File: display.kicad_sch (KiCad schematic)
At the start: 3 parts, among them J3 AXF5D3012

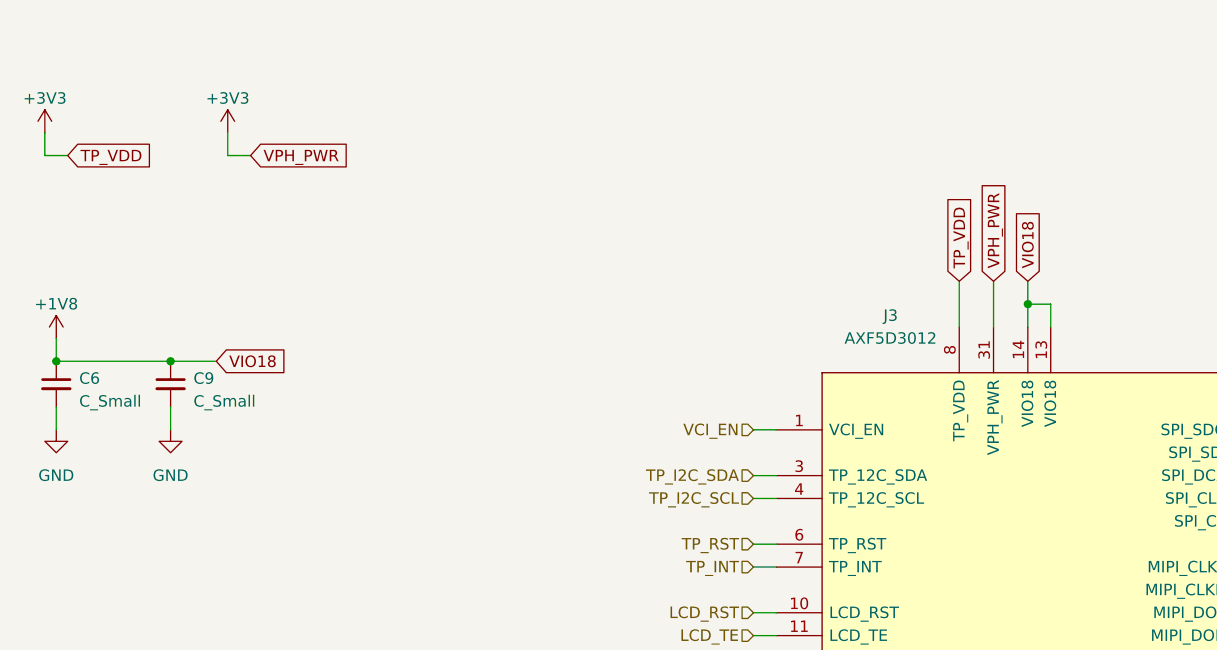
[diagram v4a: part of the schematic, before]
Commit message: cleaned up supply labels
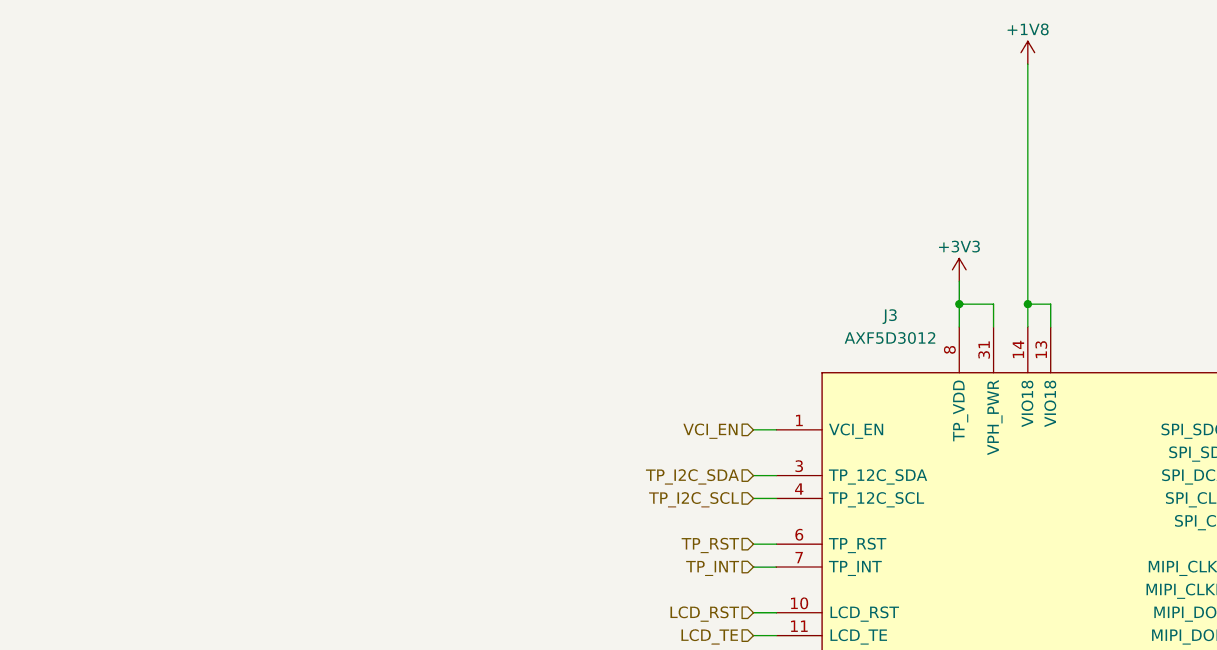
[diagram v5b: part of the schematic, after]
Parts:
- removed C6, C9: C_Small, symbol Device:C_Small

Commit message: cleaned up symbol fields table and removed unused or duplicate fields.
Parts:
- J3: MFN (none) -> 769-AXF5D3012; Manufacturer_Name Panasonic -> (none); Manufacturer_Part_Number AXF5D3012 -> (none); Mouser Part Number 769-AXF5D3012 -> (none); Mouser Price/Stock https://www.mouser.co.uk/ProductDetail/Panasonic-Industrial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 -> (none)
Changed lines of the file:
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@@
         )
         (path "/017c50c6-333c-4d31-ad5a-278994a09b14/ea4ffdec-697e-4619-8bda-0f4c7cf70f55"
-          (reference "#PWR029") (unit 1)
+          (reference "#PWR017") (unit 1)
         )
       )
@@
         )
         (path "/017c50c6-333c-4d31-ad5a-278994a09b14/ea4ffdec-697e-4619-8bda-0f4c7cf70f55"
-          (reference "#PWR013") (unit 1)
+          (reference "#PWR016") (unit 1)
         )
       )
@@
         )
         (path "/017c50c6-333c-4d31-ad5a-278994a09b14/ea4ffdec-697e-4619-8bda-0f4c7cf70f55"
-          (reference "#PWR016") (unit 1)
+          (reference "#PWR018") (unit 1)
         )
       )
@@
       (effects (font (size 1.27 1.27)) (justify left) hide)
     )
-    (property "Mouser Part Number" "769-AXF5D3012" (at 134.62 78.74 0)
-      (effects (font (size 1.27 1.27)) (justify left) hide)
-    )
-    (property "Mouser Price/Stock" "https://www.mouser.co.uk/ProductDetail/Panasonic-Industrial-Devices/AXF5D3012?qs=W0yvOO0ixfF77ugR%2FFyGrQ%3D%3D" (at 134.62 81.28 0)
-      (effects (font (size 1.27 1.27)) (justify left) hide)
-    )
-    (property "Manufacturer_Name" "Panasonic" (at 134.62 83.82 0)
-      (effects (font (size 1.27 1.27)) (justify left) hide)
-    )
-    (property "Manufacturer_Part_Number" "AXF5D3012" (at 134.62 86.36 0)
-      (effects (font (size 1.27 1.27)) (justify left) hide)
+    (property "MFN" "769-AXF5D3012" (at 113.03 71.12 0)
+      (effects (font (size 1.27 1.27)) hide)
     )
     (pin "1")

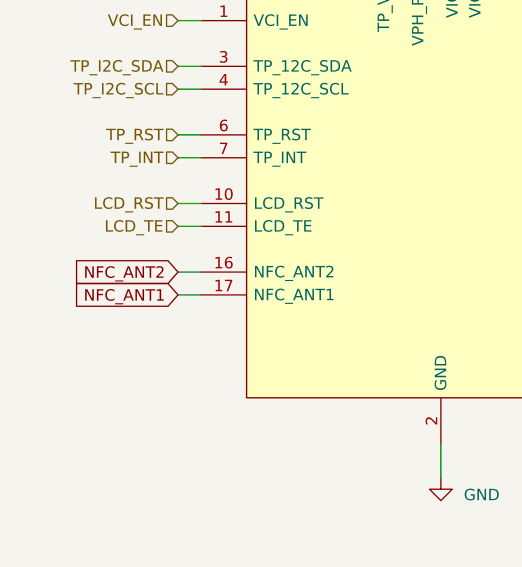
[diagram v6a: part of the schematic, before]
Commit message: added XTAL to nrf chip
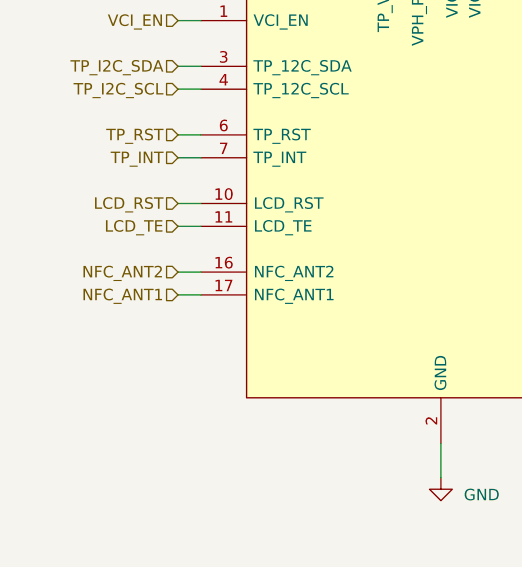
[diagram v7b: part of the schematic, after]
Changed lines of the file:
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@@
     (effects (font (size 1.5 1.5) (thickness 0.3) bold (color 255 9 33 1)) (justify left bottom))
-  )
-  (global_label "NFC_ANT2" (shape input) (at 110.49 105.41 180) (fields_autoplaced)
-    (effects (font (size 1.27 1.27)) (justify right))
-    (property "Intersheetrefs" "${INTERSHEET_REFS}" (at 98.3313 105.41 0)
-      (effects (font (size 1.27 1.27)) (justify right) hide)
-    )
-  )
-  (global_label "NFC_ANT1" (shape input) (at 110.49 107.95 180) (fields_autoplaced)
-    (effects (font (size 1.27 1.27)) (justify right))
-    (property "Intersheetrefs" "${INTERSHEET_REFS}" (at 98.3313 107.95 0)
-      (effects (font (size 1.27 1.27)) (justify right) hide)
-    )
   )
   (hierarchical_label "TP_I2C_SCL" (shape input) (at 110.49 85.09 180) (fields_autoplaced)
@@
     )
   )
+  (hierarchical_label "NFC_ANT2" (shape input) (at 110.49 105.41 180) (fields_autoplaced)
+    (effects (font (size 1.27 1.27)) (justify right))
+    (property "Intersheetrefs" "${INTERSHEET_REFS}" (at 98.3313 105.41 0)
+      (effects (font (size 1.27 1.27)) (justify right) hide)
+    )
+  )
   (hierarchical_label "SPI_SDI" (shape input) (at 171.45 80.01 0) (fields_autoplaced)
     (effects (font (size 1.27 1.27)) (justify left))
@@
       (effects (font (size 1.27 1.27)) (justify right) hide)
     )
+  )
+  (hierarchical_label "NFC_ANT1" (shape input) (at 110.49 107.95 180) (fields_autoplaced)
+    (effects (font (size 1.27 1.27)) (justify right))
+    (property "Intersheetrefs" "${INTERSHEET_REFS}" (at 98.3313 107.95 0)
+      (effects (font (size 1.27 1.27)) (justify right) hide)
+    )

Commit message: changed display footprint
- added new display_AXF5D3012.kicad_mod (from old AXF5D3012.kicad_mod)
- updated display symbol to use new footprint
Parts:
- J3: footprint ARMband:AXF5D3012 -> ARMband:display_AXF5D3012
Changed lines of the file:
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@@
       (effects (font (size 1.27 1.27)))
     )
-    (property "Footprint" "ARMband:AXF5D3012" (at 134.62 68.58 0)
+    (property "Footprint" "ARMband:display_AXF5D3012" (at 134.62 68.58 0)
       (effects (font (size 1.27 1.27)) (justify left) hide)
     )
